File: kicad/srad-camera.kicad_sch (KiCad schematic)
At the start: 17 parts, among them J1 SWD, SW1 PWRON, U1 AP63203WU

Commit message: Draft routing/layout for RK
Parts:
- removed C41: 100nF, symbol Device:C_Small
- removed R1: 22k, symbol Device:R_Small
- added R14, R15, R33, R34: 4.7k, symbol Device:R_Small
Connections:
- net GND: now also J1.3 (Pin_3), J1.5 (Pin_5), J1.9 (Pin_9); no longer J1.GND (Pin_9)
- net LSM6DSRTR/SCL: now also R34.2
- net LSM6DSRTR/SDA: now also R33.2
- net RK809-5 PMIC/SCL: now also R15.2
- net RK809-5 PMIC/SDA: now also R14.2
- net STM32U575RGT6/NRST: now also J1.10 (Pin_10); no longer J1.RST (Pin_10)
- net VSYS_3V3: now also J1.1 (Pin_1), R14.1, R15.1; no longer J1.VCC (Pin_1)
- net VIN_5V: now reaches C2.1, JST1.1 (Pin_1), U1.2 (EN), U1.3 (IN)
- net at R11.1: now also J1.4 (Pin_4); no longer J1.SWCLK (Pin_4)
- net at R32.1: now also J1.2 (Pin_2); no longer J1.SWDIO (Pin_2)
- net STM32U575RGT6/SWD1 renamed STM32U575RGT6/PA13
- net STM32U575RGT6/SWD2 renamed STM32U575RGT6/PA14
- removed net STM32U575RGT6/SWD3: J1.SWO (Pin_6)
- new net STM32U575RGT6/PB3: J1.6 (Pin_6)
- new net VCC_IMU_1V8: R33.1, R34.1
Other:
- sheet MT41K256 RAM renamed MT41K256 DDR3L
- sheet USBC 2.0 Port renamed USBC 2.0 OTG
- sheet MT41K256 DDR3L ports: added SOC_BUS?; removed none
- sheet RK3566 SoC ports: added 1, 10, 11, 12, 13, 14, 15, 16, 2, 3, 4, 5, 6, 7, 8, 9, CSI_BUS, DDR_BUS?; removed none
- sheet RK809-5 PMIC ports: added none; removed EXT_EN
- sheet STM32U575RGT6 ports: added PA13, PA14, PB12, PB13, PB3, PB6, PB7, PC0, PC1, PC2, PC3, PC6, PC7; removed IMU1, IMU2, IMU3, IMU4, PMIC1, PMIC2, PMIC3, PMIC4, PMIC5, PMIC6, SWD1, SWD2, SWD3
- note added: "ANS: No! -> STM powers on -> configs PMIC -> PWNON PMIC Means we also need to rethink VDC for PMIC"
- note added: "Can these be tied together? Noise?"
- note added: "Does this PWRON switch make any sense? Need to think about sequencing"
- note added: "WIP!"
- note added: "Which voltage do I pull SDA/SCL up to for IMU?? 3V3 or 1V8? I am assuming 1V8 since logic level for IMU. Need to check"
- moved on the sheet: BTN1, C4, FPC1, R11, R32, R?, SW1

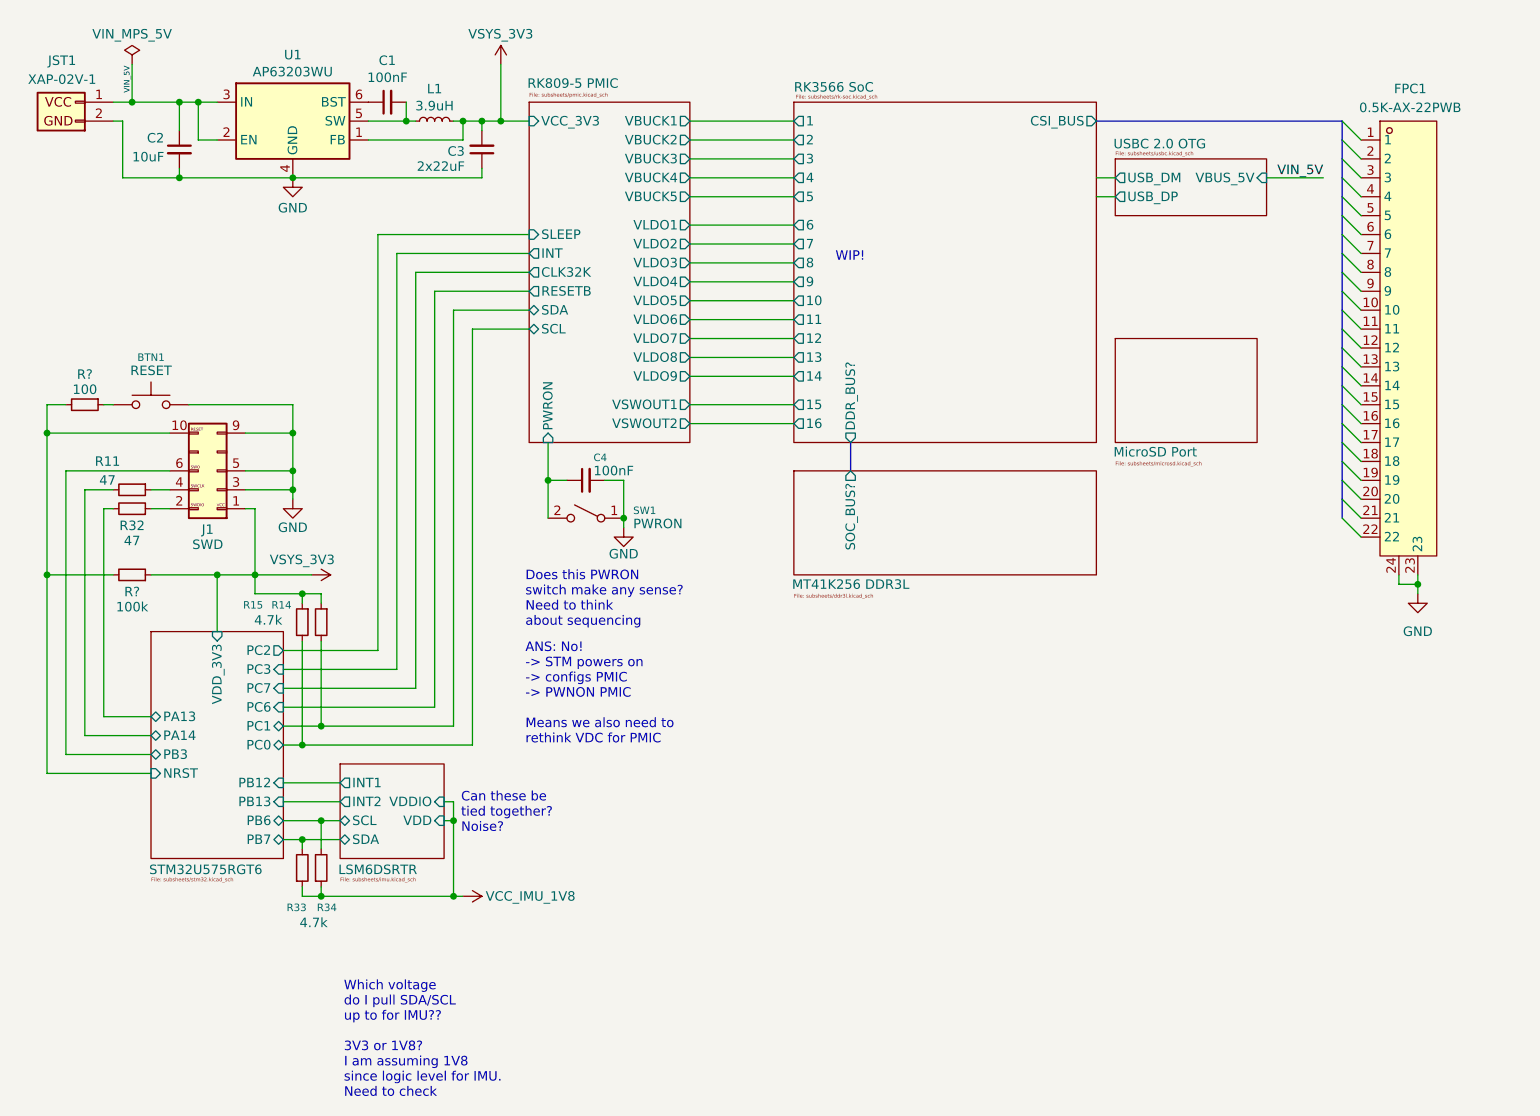
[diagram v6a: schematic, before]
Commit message: Wire microsd port
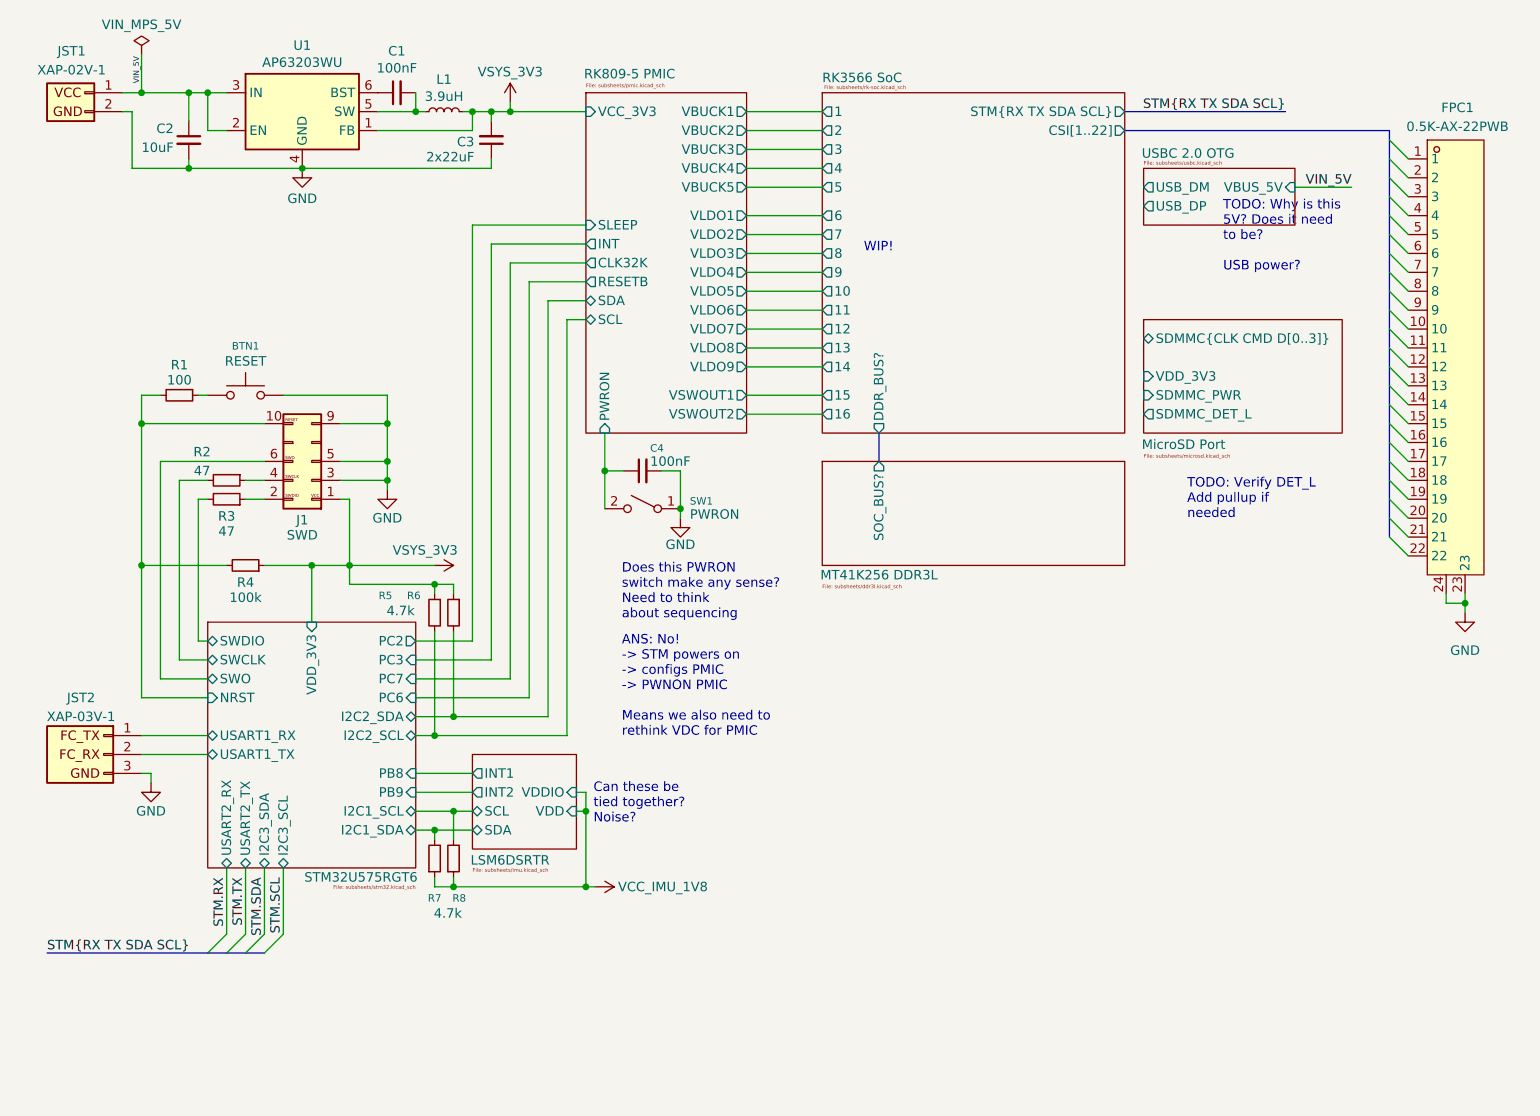
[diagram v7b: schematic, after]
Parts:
- added JST2: XAP-03V-1, symbol Connector_Generic:Conn_01x03
- gave numbers to parts that had none: 2
- renumbered R11 to R2, R32 to R3, R15 to R5, R14 to R6, R33 to R7, R34 to R8
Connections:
- net GND: now also JST2.3 (Pin_3)
- net STM32U575RGT6/PA13 renamed STM32U575RGT6/SWDIO
- net STM32U575RGT6/PA14 renamed STM32U575RGT6/SWCLK
- net STM32U575RGT6/PB3 renamed STM32U575RGT6/SWO
- new net STM32U575RGT6/USART1_RX: JST2.1 (Pin_1)
- new net STM32U575RGT6/USART1_TX: JST2.2 (Pin_2)
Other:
- sheet MicroSD Port ports: added SDMMC_DET_L, SDMMC_PWR, SDMMC{CLK CMD D[0..3]}, VDD_3V3; removed none
- sheet RK3566 SoC ports: added CSI[1..22], STM{RX TX SDA SCL}; removed CSI_BUS
- sheet STM32U575RGT6 ports: added I2C1_SCL, I2C1_SDA, I2C2_SCL, I2C2_SDA, I2C3_SCL, I2C3_SDA, PB8, PB9, SWCLK, SWDIO, SWO, USART1_RX, USART1_TX, USART2_RX, USART2_TX; removed PA13, PA14, PB12, PB13, PB3, PB6, PB7, PC0, PC1
- note added: "TODO: Verify DET_L Add pullup if needed"
- note added: "TODO: Why is this 5V? Does it need to be? USB power?"
- note removed: "Which voltage do I pull SDA/SCL up to for IMU?? 3V3 or 1V8? I am assuming 1V8 since logic level for IMU. Need to check"
- moved on the sheet: BTN1, C1, C2, C3, C4, FPC1, J1, JST1, L1, R1, R2, R3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

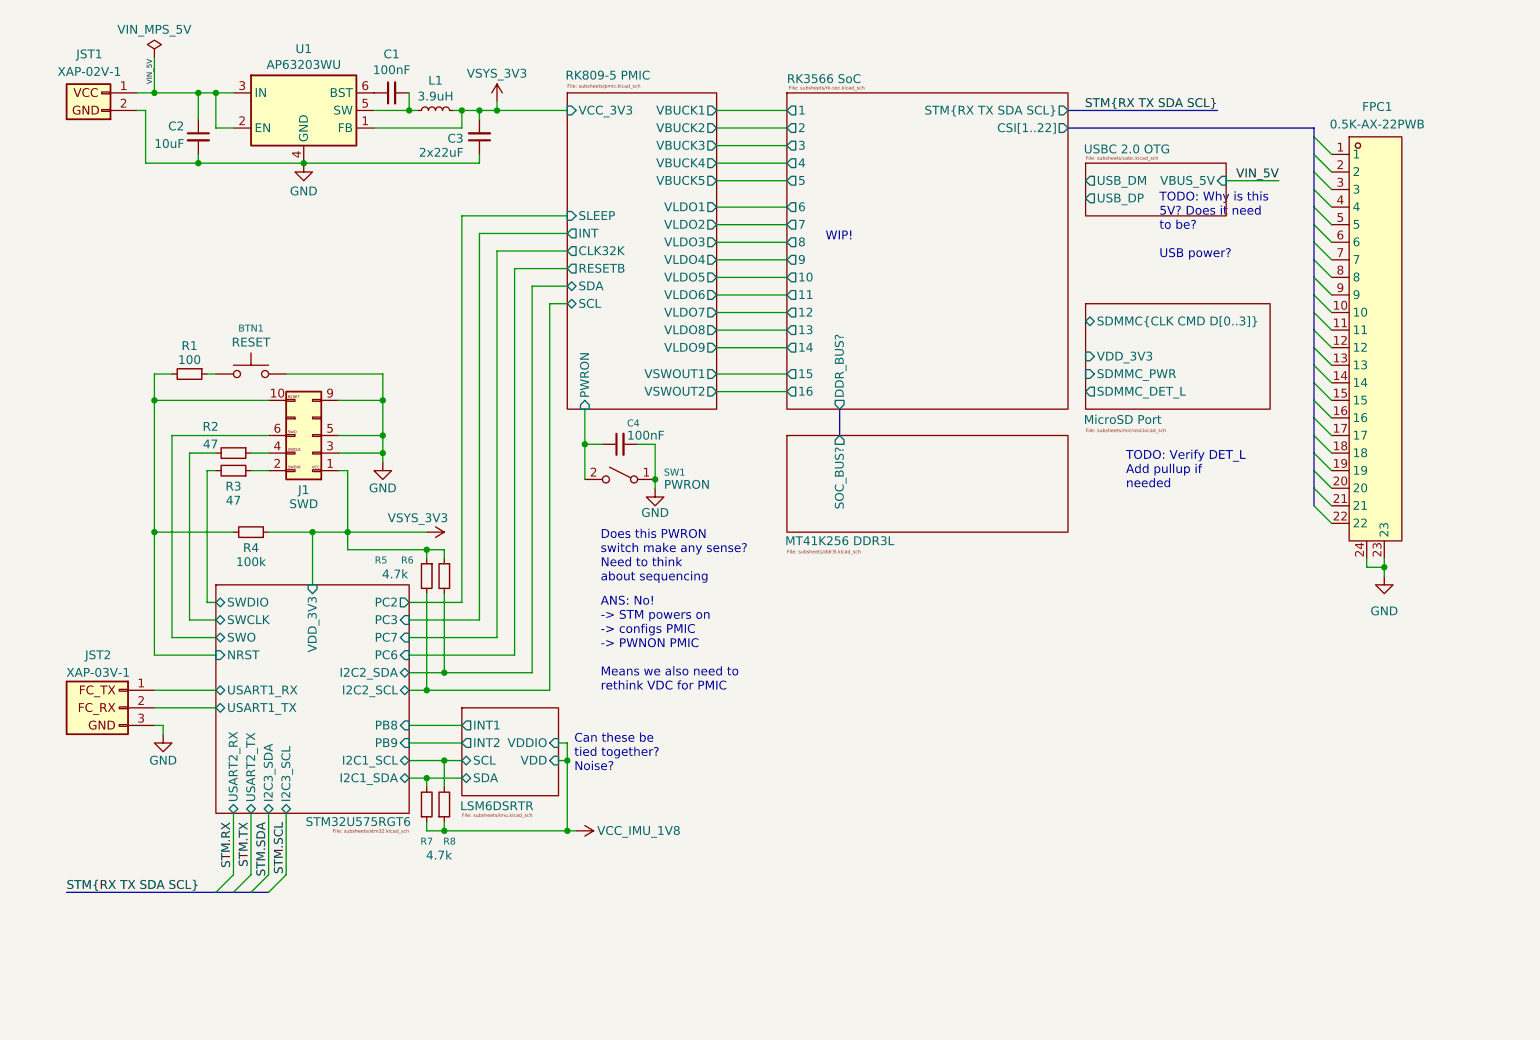
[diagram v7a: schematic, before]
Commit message: Clean up root sheet, add power supply subsheet
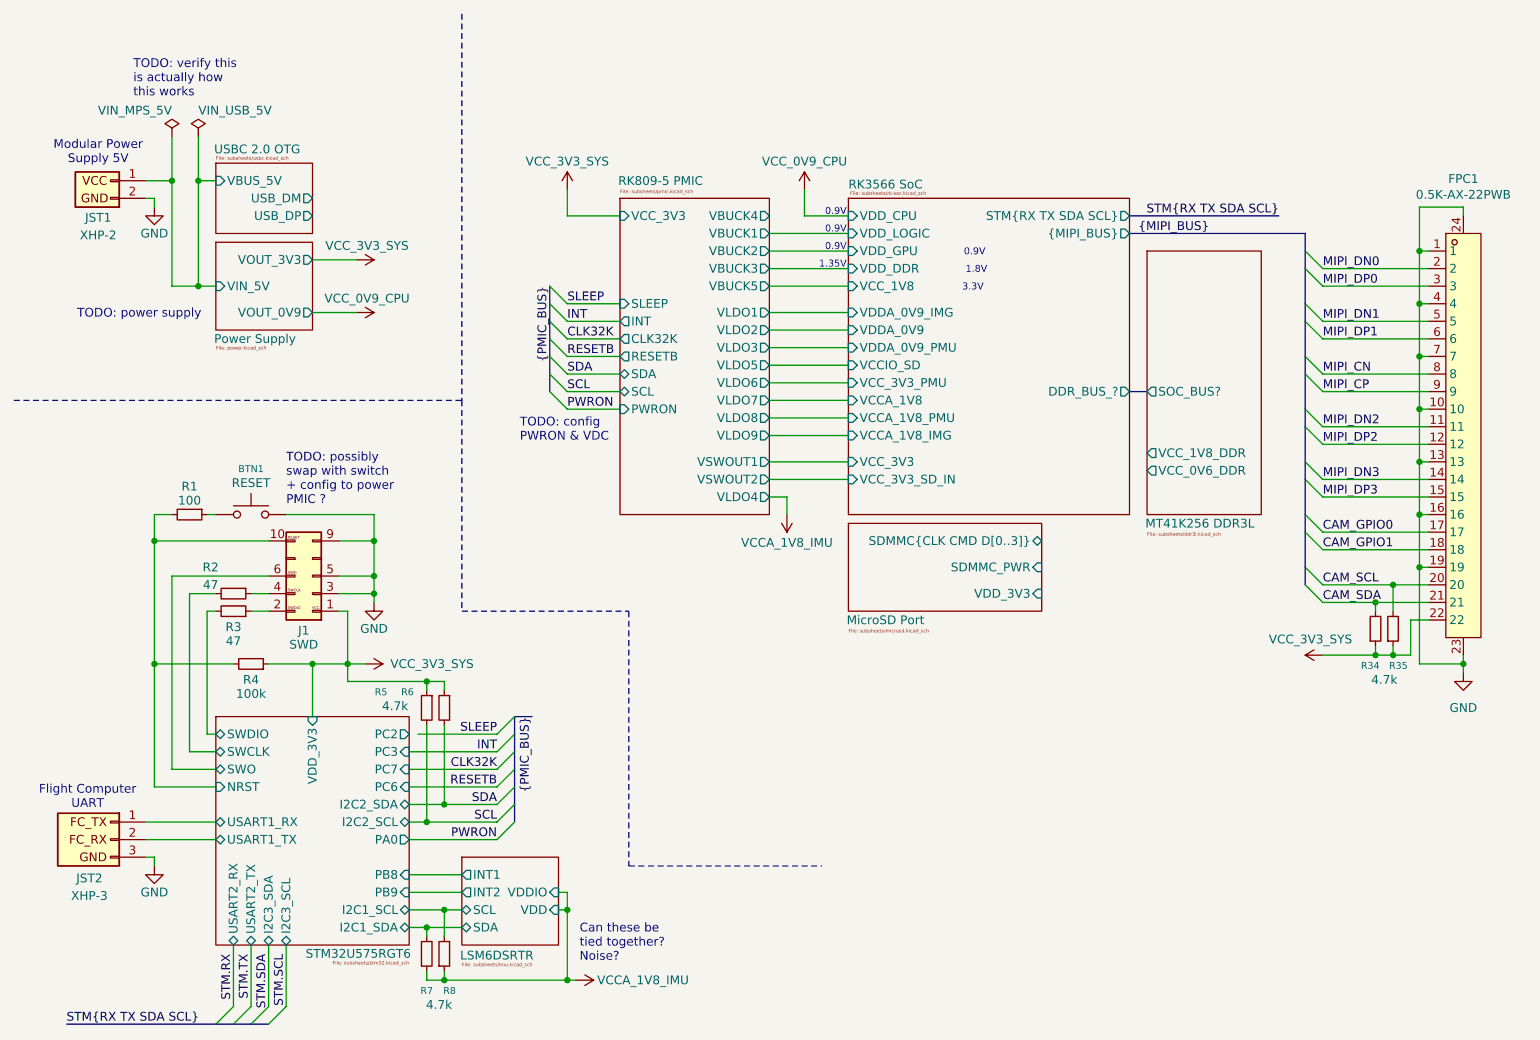
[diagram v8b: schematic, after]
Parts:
- removed C1, C4: 100nF, symbol Device:C_Small
- removed C2: 10uF, symbol Device:C_Small
- removed C3: 2x22uF, symbol Device:C_Small
- removed L1: 3.9uH, symbol Device:L_Small
- removed SW1: PWRON, symbol Switch:SW_SPST
- removed U1: AP63203WU, Package_TO_SOT_SMD:TSOT-23-6, symbol Regulator_Switching:AP63203WU
- added R34, R35: 4.7k, symbol Device:R_Small
- JST1: value XAP-02V-1 -> XHP-2
- JST2: value XAP-03V-1 -> XHP-3
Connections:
- net VSYS_3V3 is gone; now on net VCC_3V3_SYS: J1.1 (Pin_1), R4.1, R5.1, R6.1
- net GND: now also FPC1.1, FPC1.10, FPC1.13, FPC1.16, FPC1.19, FPC1.4, FPC1.7
- net MIPI_DN2: now reaches FPC1.11
- net MIPI_DP2: now reaches FPC1.12
- net MIPI_DN3: now reaches FPC1.14
- net MIPI_DP3: now reaches FPC1.15
- net CAM_GPIO0: now reaches FPC1.17
- net CAM_GPIO1: now reaches FPC1.18
- net MIPI_DN0: now reaches FPC1.2
- net CAM_SCL: now reaches FPC1.20
- net CAM_SCL: now also R35.2
- net CAM_SDA: now reaches FPC1.21
- net CAM_SDA: now also R34.2
- net VCC_3V3_SYS: now reaches FPC1.22
- net VCC_3V3_SYS: now also R34.1, R35.1
- net MIPI_DP0: now reaches FPC1.3
- net MIPI_DN1: now reaches FPC1.5
- net MIPI_DP1: now reaches FPC1.6
- net MIPI_CN: now reaches FPC1.8
- net MIPI_CP: now reaches FPC1.9
- net RK809-5 PMIC/SCL renamed SCL
- net RK809-5 PMIC/SDA renamed SDA
- net VCC_IMU_1V8 renamed VCCA_1V8_IMU
- net VIN_5V renamed Power Supply/VIN_5V
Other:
- added sheet Power Supply (power.kicad_sch)
- sheet MT41K256 DDR3L ports: added VCC_0V6_DDR, VCC_1V8_DDR; removed none
- sheet MicroSD Port ports: added none; removed SDMMC_DET_L
- sheet RK3566 SoC ports: added DDR_BUS_?, VCCA_1V8, VCCA_1V8_IMG, VCCA_1V8_PMU, VCCIO_SD, VCC_1V8, VCC_3V3, VCC_3V3_PMU, VCC_3V3_SD_IN, VDDA_0V9, VDDA_0V9_IMG, VDDA_0V9_PMU, VDD_CPU, VDD_DDR, VDD_GPU, VDD_LOGIC, {MIPI_BUS}; removed 1, 10, 11, 12, 13, 14, 15, 16, 2, 3, 4, 5, 6, 7, 8, 9, CSI[1..22], DDR_BUS?
- sheet STM32U575RGT6 ports: added PA0; removed none
- note added: "0.9V"
- note added: "1.35V"
- note added: "1.8V"
- note added: "3.3V"
- note added: "Flight Computer UART"
- note added: "Modular Power Supply 5V"
- note added: "TODO: config PWRON & VDC"
- note added: "TODO: possibly swap with switch + config to power PMIC ?"
- note added: "TODO: power supply"
- note added: "TODO: verify this is actually how this works"
- note removed: "ANS: No! -> STM powers on -> configs PMIC -> PWNON PMIC Means we also need to rethink VDC for PMIC"
- note removed: "Does this PWRON switch make any sense? Need to think about sequencing"
- note removed: "TODO: Verify DET_L Add pullup if needed"
- note removed: "TODO: Why is this 5V? Does it need to be? USB power?"
- note removed: "WIP!"
- moved on the sheet: BTN1, J1, JST1, JST2, R1, R2, R3, R4, R5, R6, R7, R8
